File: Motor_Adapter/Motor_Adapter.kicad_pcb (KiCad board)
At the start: 2 copper layers, 53 x 32 mm, 6 parts, among them J2 Windings, J3 Hall_Sensor, J5 Windings, J6 Hall_Sensor, K1 Maxon-200142, K2 Maxon-200142

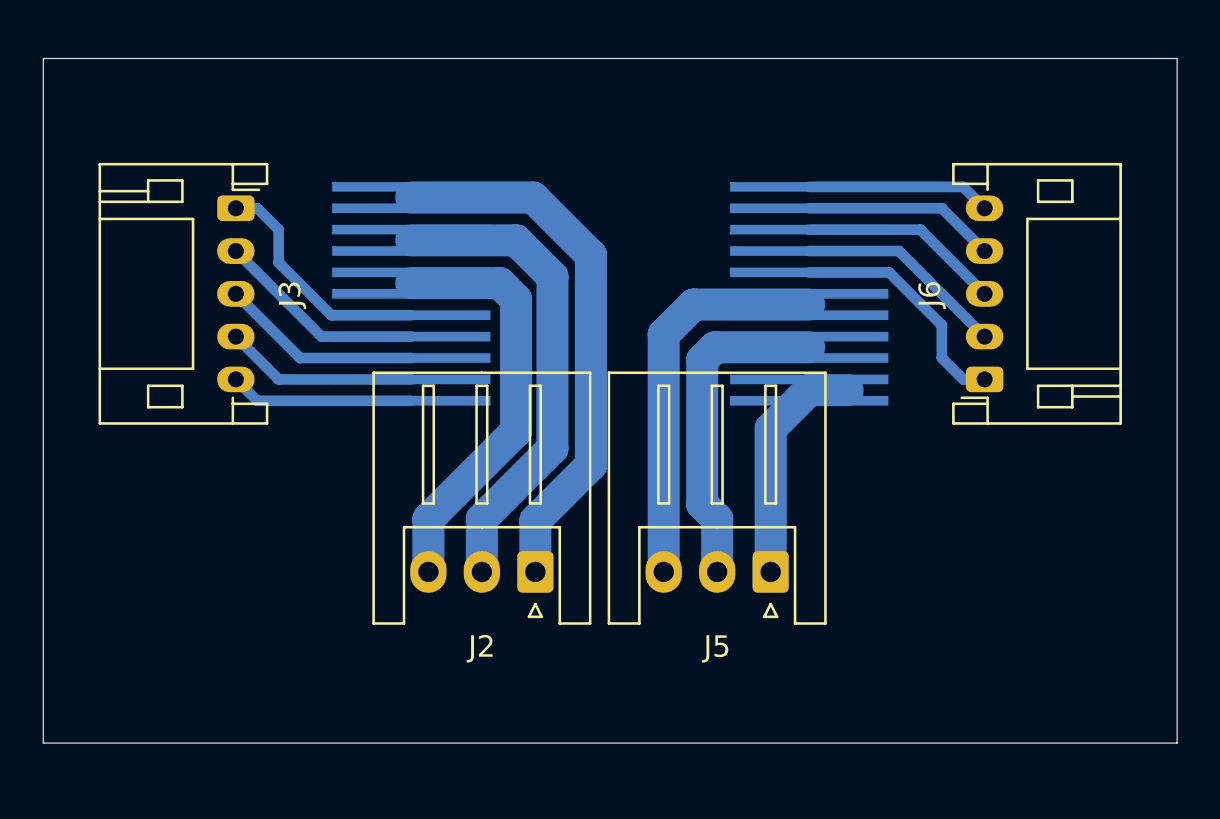
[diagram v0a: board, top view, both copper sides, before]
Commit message: modif de la carte d'adaptation pour les moteurs
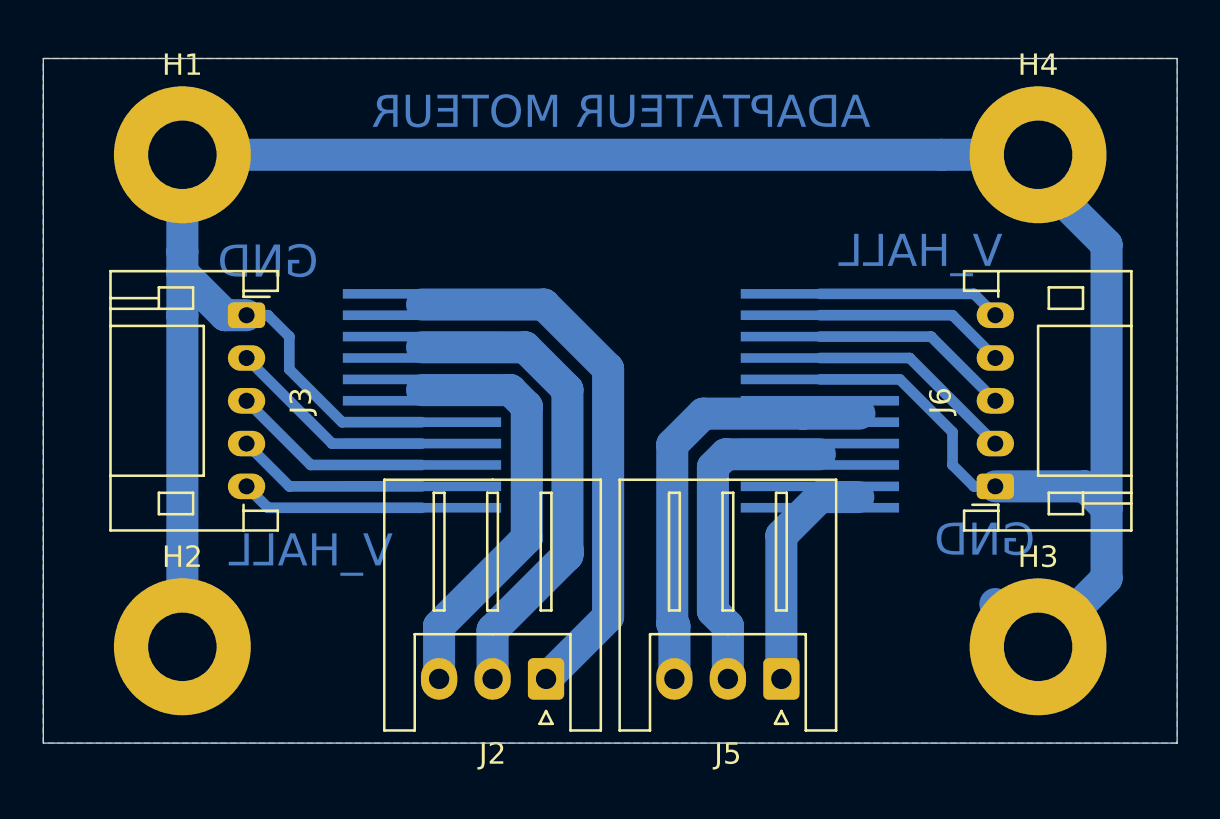
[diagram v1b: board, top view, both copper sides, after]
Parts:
- added H1: MountingHole_Pad, MountingHole:MountingHole_3.2mm_M3_Pad, F.Cu at (99.5, 104.5)
- added H2: MountingHole_Pad, MountingHole:MountingHole_3.2mm_M3_Pad, F.Cu at (99.5, 127.5)
- added H3: MountingHole_Pad, MountingHole:MountingHole_3.2mm_M3_Pad, F.Cu at (139.5, 127.5)
- added H4: MountingHole_Pad, MountingHole:MountingHole_3.2mm_M3_Pad, F.Cu at (139.5, 104.5)
- moved J2 5.02 mm to (116.5, 129.0)
- moved J3 5.02 mm to (102.5, 112.0)
- moved J5 5.02 mm to (127.5, 129.0)
- moved J6 5.02 mm to (137.5, 120.0)
- moved K1 5.02 mm to (110.5, 116.0)
- moved K2 5.02 mm to (129.5, 116.0)
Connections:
- J3 pad 1: Net-(J3-Pad1) -> GND
- J6 pad 1: Net-(J6-Pad1) -> GND
- K1 pad 7: Net-(J3-Pad1) -> GND
- K2 pad 7: Net-(J6-Pad1) -> GND
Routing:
- net GND: track 0.00 -> 123.3 mm
- net Net-(J3-Pad1): track 11.2 -> 0.00 mm
- net Net-(J6-Pad1): track 11.2 -> 0.00 mm
- net Net-(J2-Pad1): track 34.4 -> 26.1 mm
- net Net-(J5-Pad3): track 19.0 -> 20.3 mm
- added copper zone on B.Cu, net GND
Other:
- net class Default: clearance 0.2 -> 0.4
- rule trace_clearance: 0.2 -> 0.4
- board text added: "ADAPTATEUR MOTEUR"
- board text added: "GND"
- board text added: "V_HALL"
